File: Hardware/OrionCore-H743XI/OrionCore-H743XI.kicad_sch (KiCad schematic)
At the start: 0 parts

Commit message: feat: update dual qspi
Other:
- company: (none) -> Peakors
- title: (none) -> OrionCore
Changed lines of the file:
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@@
 	(generator_version "10.0")
 	(paper "A4")
+	(title_block
+		(title "OrionCore")
+		(date "2026-05-15")
+		(rev "V1.0")
+		(company "Peakors")
+	)
 	(sheet
 		(at 26.67 133.985)
@@
 	)
 	(embedded_fonts no)
+	(embedded_files
+		(file
+			(name "KCA_A4_01.kicad_wks")
+			(type worksheet)
+			(data |KLUv/WDqCf0VAJZeYCAAmRtW2iRDK2TDlpqBLyKcpyVzUk48cVMDJLP0/081IVYAUABbAN95BvE/
+				5kL8opDNUfa1oVzBz4P8M1CJxRa9Z1F+7WegmGxf2dKn/AsAQEAQmt5LEWtcn8t6/vnCqzP+mv16
+				yMCQUiJmnH2xLWU/FQABQYmE+ni1s6RCHTmOixJRAPzFINl0dgmHl7z6U/7c04igsyNVpXJ37VcP
+				PWe/GXf/dex4kTr8ce3f228XfXvXhHPtq/86COJu9mzvegLRUcr+XL90Xe1gvQFXfwUzBnX2sGY0
+				WibL+MpuvA9zncDipKNpTq5hMK6mSCzRjSgvmMlGo3U+kOwxobAIFKMdpWxgil4wWtqWQT4aZ7OZ
+				sAjt8K+QnLMq+1/vWgWyXzKN6GyZqSYNAYFh0kWcikkbMmKMGSmWkNtFs6huDUH8aEk9lyxjwTwy
+				Fr0pk5Ity2yaJtkgEFiUluyiVSYRG+nsV9/2jHGBMWbPGCOmVbbJ9r3dpvRsv7tosxgcWoNQzQSA
+				iaARQaWYmRIpSJIUOmBExMxVN2ahAouCwwNY6fYQ+S+Ti21pT5JuQhiEtZ/LPWilfuW72oO2wfGD
+				ISYoYqAsO8In6xomq5F/mRxt5gaAj9ccKnBCfQ1CXB3MgGs964/IIjYtS/2HDxjv1u1g7+dZRMw2
+				r/WdaFRPoEsELZnnLARVXgIVYlFnXyhEBPyL8Ea5slwEM2vN4UsHOeokVIPFuy0adoUtSqQcjYZp
+				lzINk5Xj1EF8QH/Kxdi2kDNm+Og9q2FMR5/40KikzUQOe8ptFLWXzpr6w4EQzSn1iWYlL47gAb95
+				gmO1J0DmmJVb6Pj3Xhm2rcuhXxAYaRVJ6cFNRFgBhgPgTyeJKREslqKH6VcDhgOHWT1a7mzRTbrF
+				CbmMiOCnc2JvU6JNnaYNa/0bnkvcWPY6SMcAVwE=|
+			)
+			(checksum "43FDF5989D8FB9E8D56AEAEA202998C9")
+		)
+	)
 )

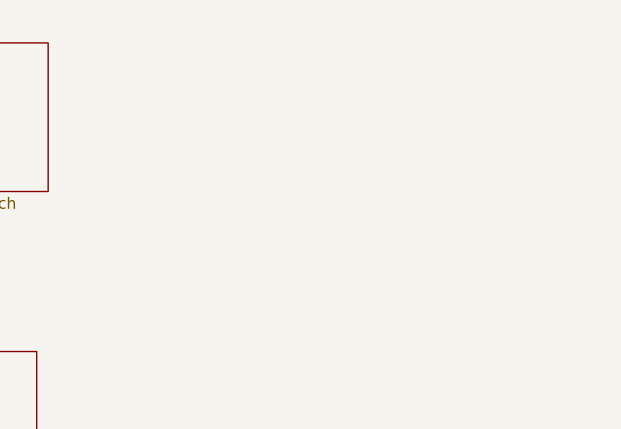
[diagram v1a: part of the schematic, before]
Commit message: feat:update j-link connect 19pin 1.27mm
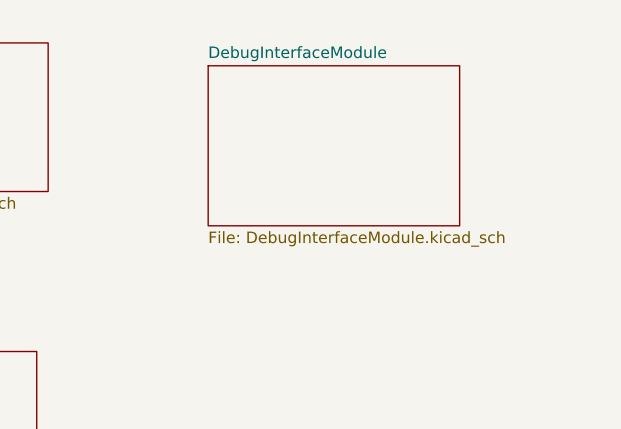
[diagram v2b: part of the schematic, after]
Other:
- added sheet DebugInterfaceModule (DebugInterfaceModule.kicad_sch)
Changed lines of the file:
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@@
+	)
+	(sheet
+		(at 73.66 31.75)
+		(size 27.94 17.78)
+		(exclude_from_sim no)
+		(in_bom yes)
+		(on_board yes)
+		(dnp no)
+		(fields_autoplaced yes)
+		(stroke
+			(width 0.1524)
+			(type solid)
+		)
+		(fill
+			(color 0 0 0 0)
+		)
+		(property "Sheetname" "DebugInterfaceModule"
+			(at 73.66 31.0384 0)
+			(show_name no)
+			(do_not_autoplace no)
+			(effects
+				(font
+					(size 1.27 1.27)
+				)
+				(justify left bottom)
+			)
+		)
+		(property "Sheetfile" "DebugInterfaceModule.kicad_sch"
+			(at 73.66 50.1146 0)
+			(show_name no)
+			(do_not_autoplace no)
+			(effects
+				(font
+					(size 1.27 1.27)
+				)
+				(justify left top)
+			)
+		)
+		(instances
+			(project "OrionCore-H743XI"
+				(path "/02115977-f748-4728-9543-88d4a684aec9"
+					(page "6")
+				)
+			)
+		)
 	)
 	(sheet
